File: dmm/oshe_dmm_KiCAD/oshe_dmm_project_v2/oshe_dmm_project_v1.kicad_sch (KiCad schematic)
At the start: 99 parts, among them J1 FTDI Basic, J10 Voltage Range 2, J11 Voltage Range 3, J12 Voltage Range 3, J13 DC Current Indication, J14 Continuity, J16 AC Voltage Range 2, J18 AC Voltage Range 3, J2 Voltage, J20 AC Voltage Range 1, J21 AC Current Indication, J22 MJ-3536N, J23 Reset, J24 D13, J25 D11, J26 D12, J3 GND, J4 Current, J5 Resistance Meas, J6 ON/OFF, J7 Voltage Range 1, J8 Voltage Range 1, J9 Voltage Range 2, SW1 PTS526 SK15 SMTR2 LFS, U1 ATmega328P-A, U2 AD736, U3 ADS1115IDGS, U4 MAX4617CPE, U5 LM317_SOT-223, U7 TPS60400DBV, U8 ADS1115IDGS, Y1 16MHz

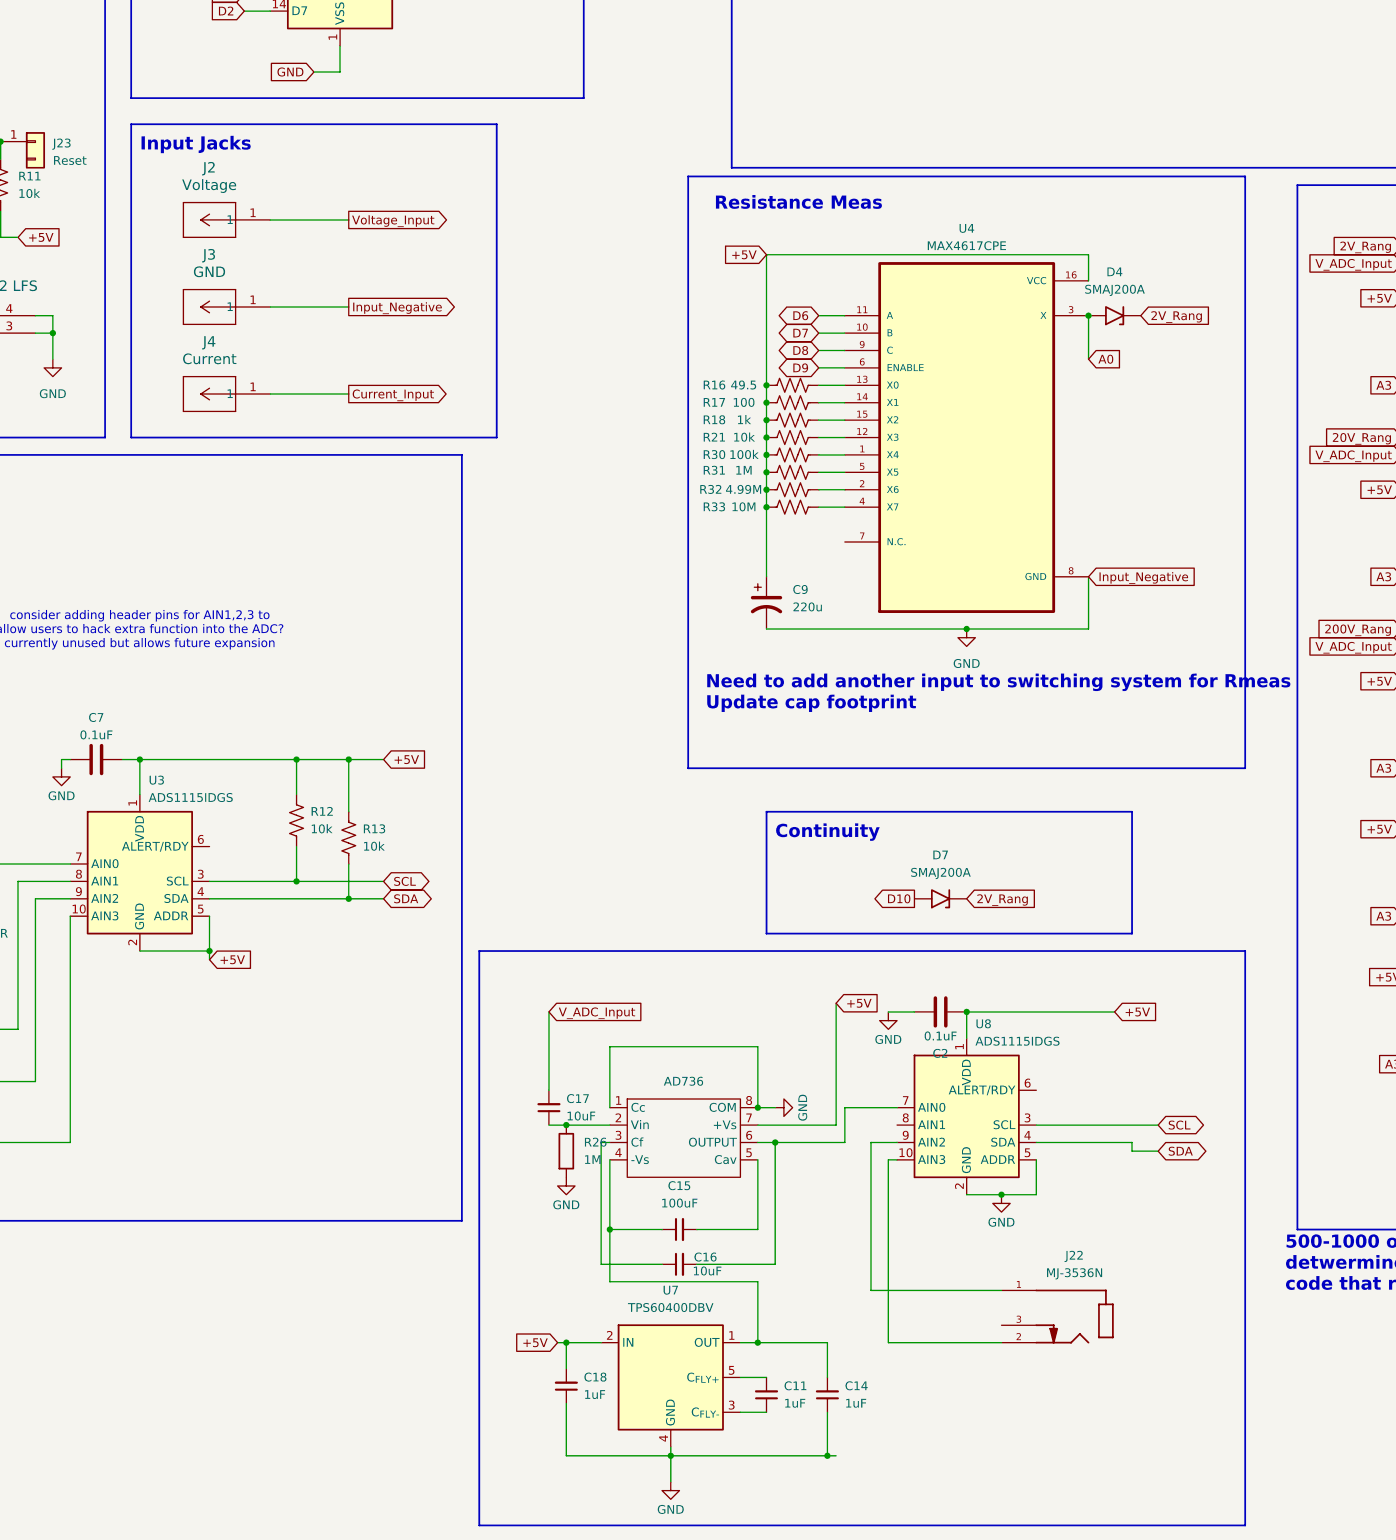
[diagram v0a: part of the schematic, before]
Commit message: Added New Input Probe
Added a new input probe for resistance measurement. Also fixed the direction of some polarized capacitors.
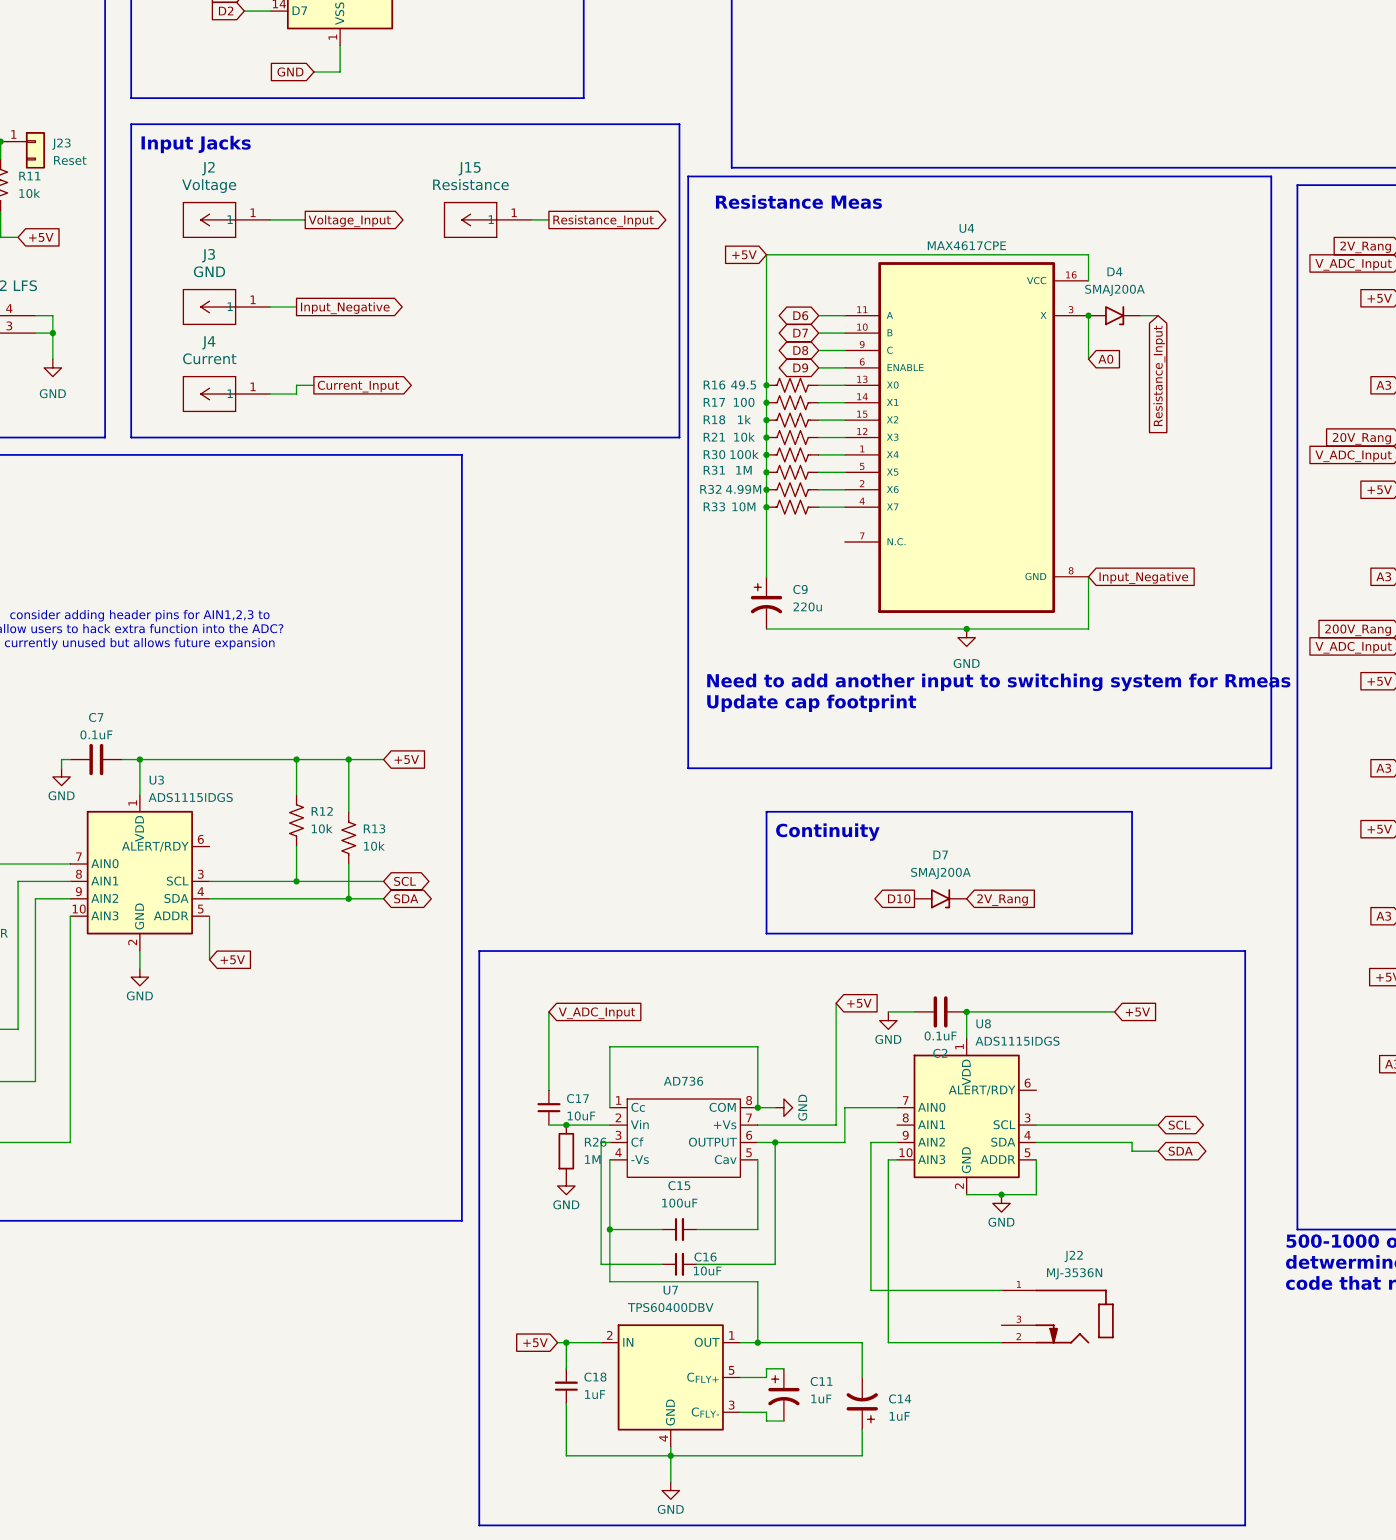
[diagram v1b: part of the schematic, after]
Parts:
- removed C11, C14: 1uF, Capacitor_SMD:CP_Elec_4x4.5, symbol Device:C_Small
- added C11, C14: 1uF, Capacitor_SMD:CP_Elec_4x4.5, symbol Device:C_Polarized_US
- added J15: Resistance, DMM_Footprint_Library:CONN_575-8_KEY, symbol DMM_Symbol_Library:575-8
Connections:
- net +5V: no longer U3.2 (GND)
- net 2V_Rang: no longer D4.1 (A1)
- net GND: now also U3.2 (GND), C14.1
- net at C15.1, U2.4 (-Vs), U7.1 (OUT): now also C14.2
- net at U7.3 (C_{FLY-}): now also C11.2
- net at U7.5 (C_{FLY+}): now also C11.1
- new net Resistance_Input: D4.1 (A1), J15.1
